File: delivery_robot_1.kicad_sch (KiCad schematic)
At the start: 29 parts, among them J1 SWD, J11 IMU I2C (STEMMA QT), J12 IMU INT/RST, J2 XT30PW-M, J4 BOOT0 jumper, J5 Conn_01x03_Pin, J6 MDD20A PWM1/DIR1/GND, J7 Motor1 encoder, SW1 RESET, U1 STM32F091RCTx, Y3 8MHz

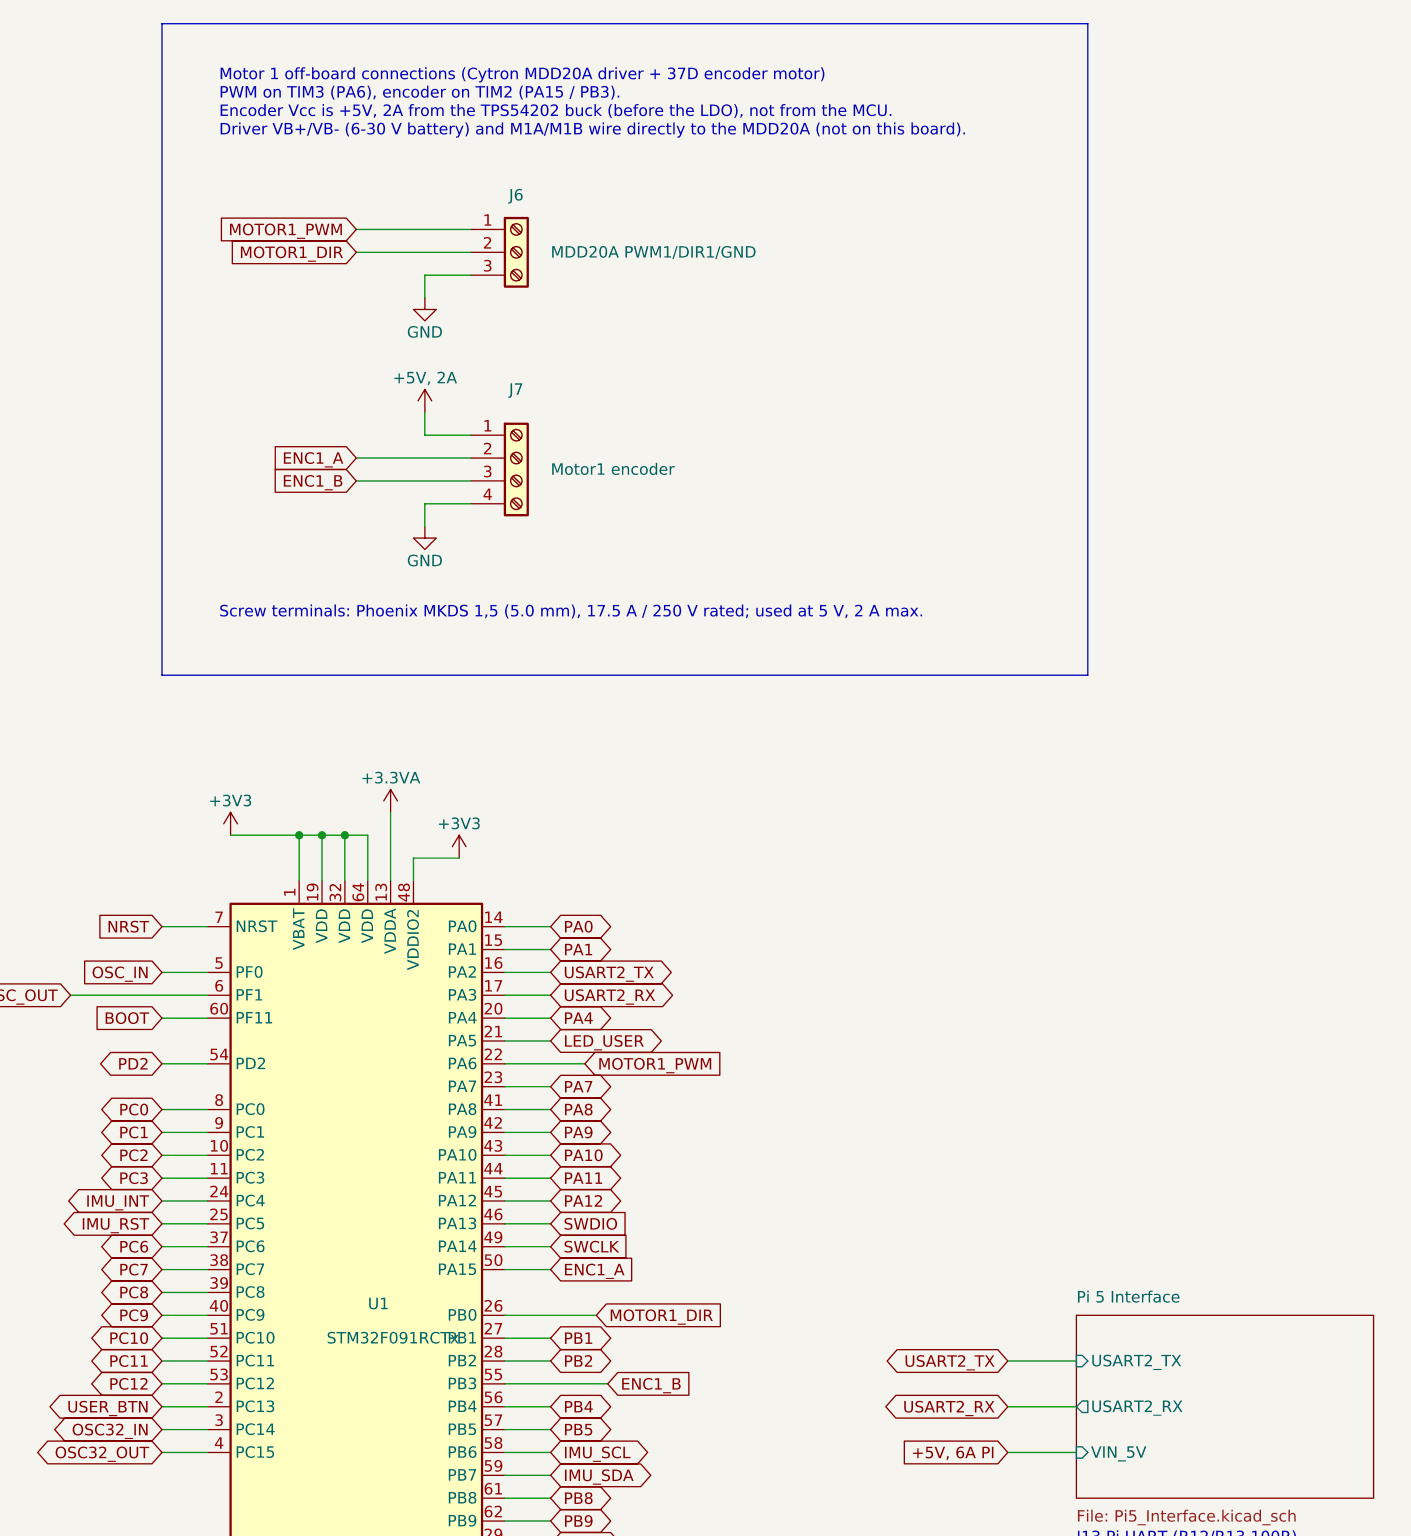
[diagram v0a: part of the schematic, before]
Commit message: Add motor 2 channel and move motor I/O to a Motor Control sheet
New Motor_Control.kicad_sch sheet (page 9) holds both channels of the
Cytron MDD20A driver and both 37D encoder connectors:
- Motor 1, moved unchanged: J6 (PWM1/DIR1/GND) and J7 (+5V 2A, A, B,
  GND)
- Motor 2, new: J16 (PWM2/DIR2/GND, Phoenix 1715035 like J6) and J15
  (encoder, same as J7)

STM32 pins:
  MOTOR1_PWM PA6 TIM3_CH1, MOTOR1_DIR PB0, ENC1_A/B PA15/PB3 (TIM2)
  MOTOR2_PWM PA7 TIM3_CH2, MOTOR2_DIR PB2, ENC2_A/B PA8/PA9 (TIM1)
Both PWMs share TIM3 (same frequency, <= 20 kHz for the MDD20A); each
encoder has its own timer in encoder mode.

The pins are shown in three places: 8 sheet pins on the root block
plus a summary note under it, a full pin and timer table inside the
sheet, and the connector descriptions. PA7/PB2/PA8/PA9 global labels
are renamed at U1 and on the J8/J9 breakout headers.

Motor 1 connectivity is unchanged; apart from J15/J16 the netlist is
identical.
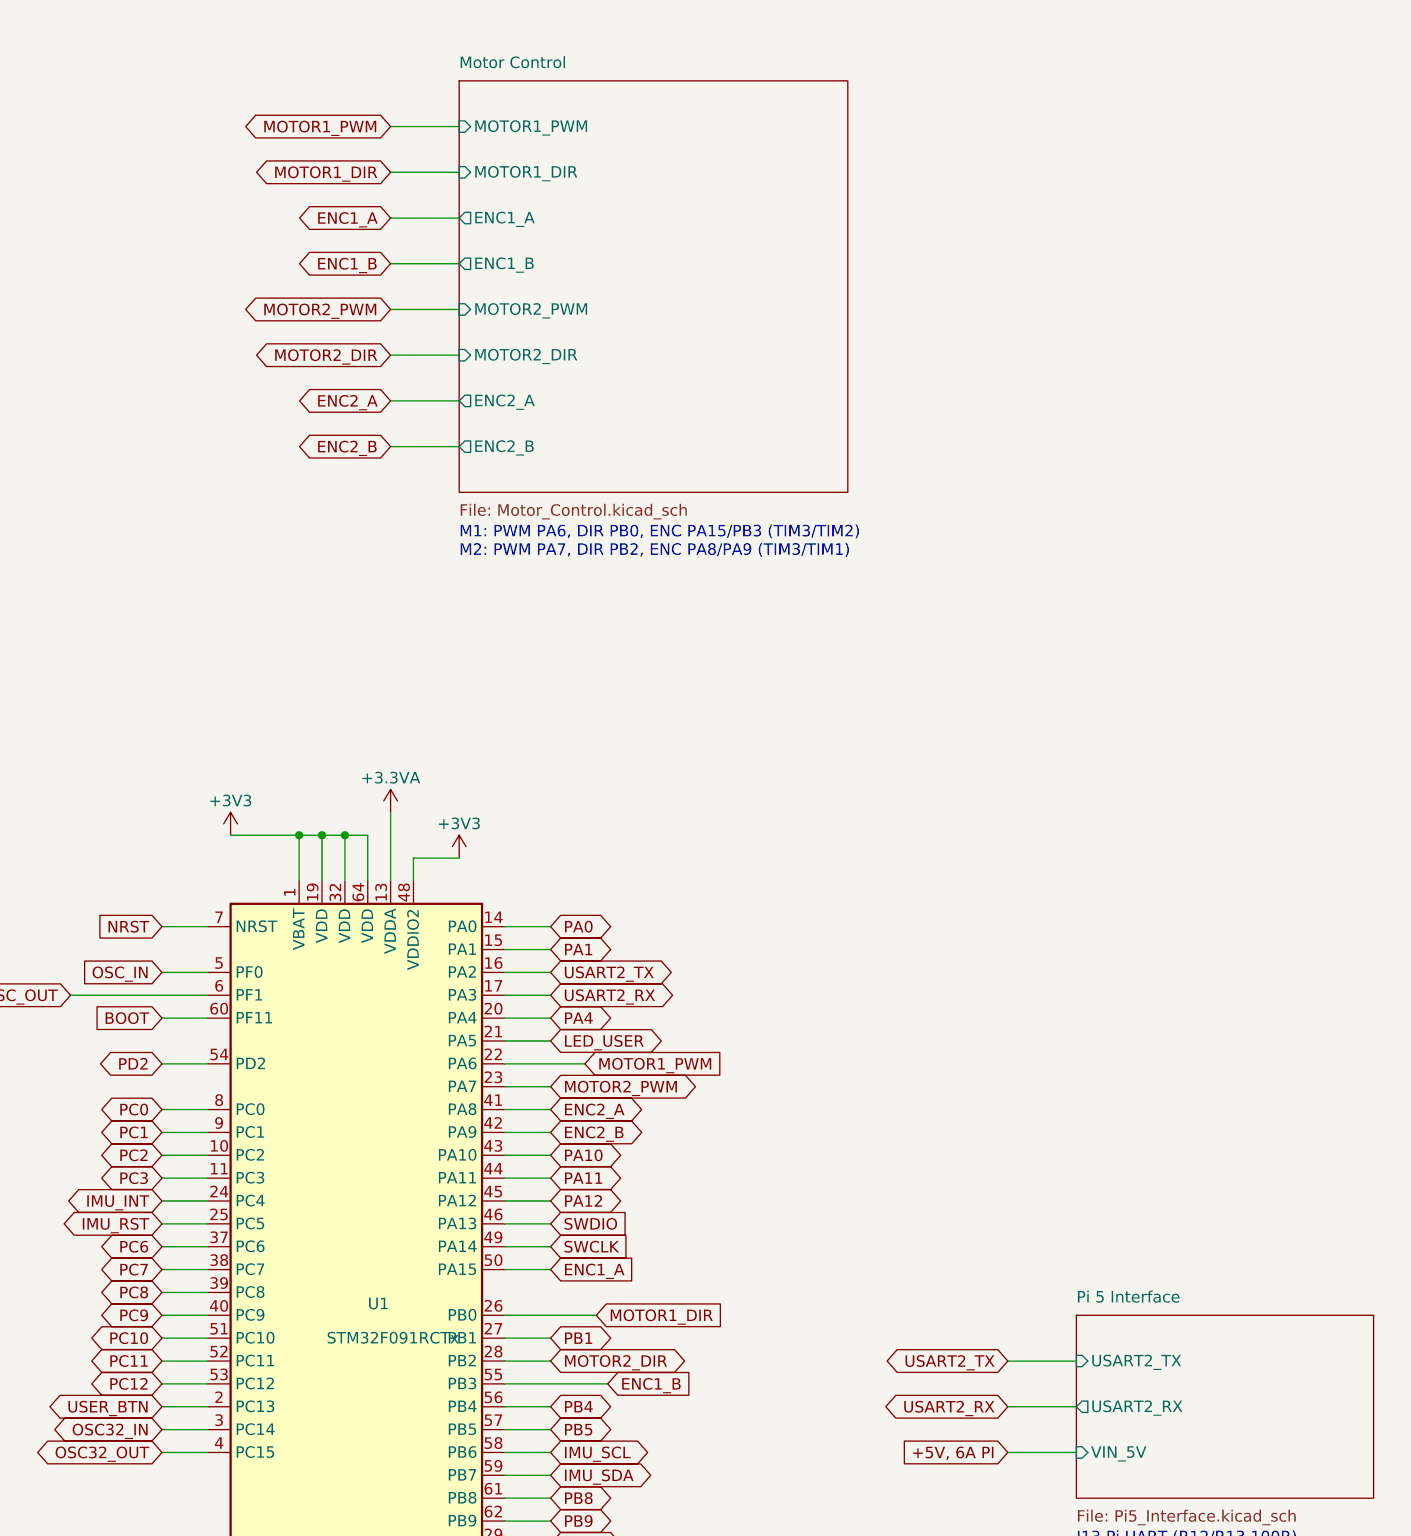
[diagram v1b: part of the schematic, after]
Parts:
- removed J6: MDD20A PWM1/DIR1/GND, TerminalBlock_Phoenix:TerminalBlock_Phoenix_MKDS-1,5-3_1x03_P5.00mm_Horizontal, symbol Connector:Screw_Terminal_01x03
- removed J7: Motor1 encoder, TerminalBlock_Phoenix:TerminalBlock_Phoenix_MKDS-1,5-4_1x04_P5.00mm_Horizontal, symbol Connector:Screw_Terminal_01x04
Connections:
- net PA7 renamed MOTOR2_PWM
- net PA8 renamed ENC2_A
- net PA9 renamed ENC2_B
- net PB2 renamed MOTOR2_DIR
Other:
- added sheet Motor Control (Motor_Control.kicad_sch)
- note added: "M1: PWM PA6, DIR PB0, ENC PA15/PB3 (TIM3/TIM2) M2: PWM PA7, DIR PB2, ENC PA8/PA9 (TIM3/TIM1)"
- note removed: "Motor 1 off-board connections (Cytron MDD20A driver + 37D encoder motor) PWM on TIM3 (PA6), encoder on TIM2 (PA15 / PB3). Encoder Vcc is +5V, 2A from the TPS54202 buck (before the LDO), not from the MCU. Driver VB+/VB- (6-30 V battery) and M1A/M1B wire directly to the MDD20A (not on this board)."
- note removed: "Screw terminals: Phoenix MKDS 1,5 (5.0 mm), 17.5 A / 250 V rated; used at 5 V, 2 A max."
